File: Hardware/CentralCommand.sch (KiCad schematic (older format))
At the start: 15 parts, among them IC101 STM32F030C8, P101 SERIAL, P102 I2C, P103 SPI, P104 ADC, Y101 Crystal_Small

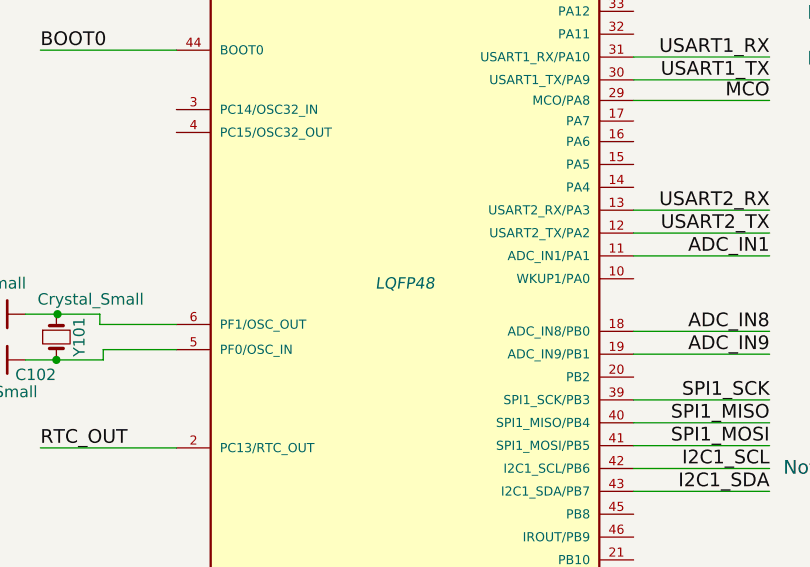
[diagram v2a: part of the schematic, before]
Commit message: initial footprint assignments
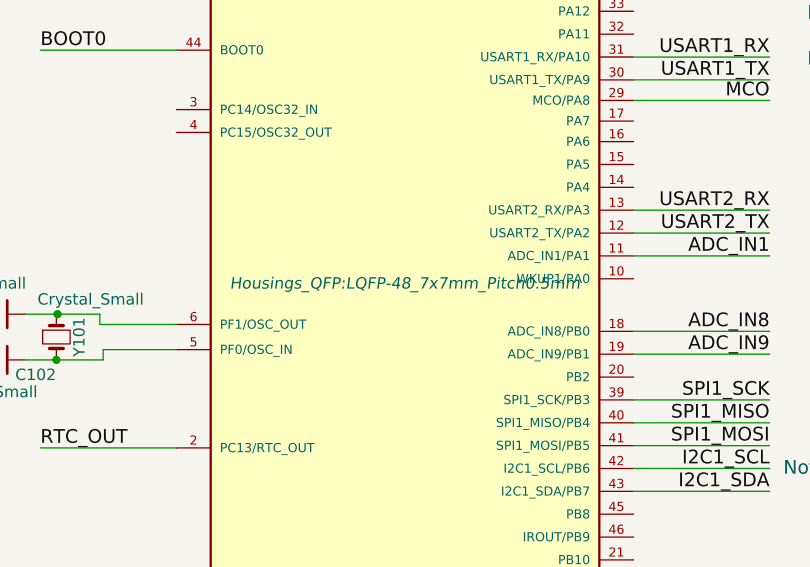
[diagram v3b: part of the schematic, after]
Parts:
- C101, C102, C104, C105, C106, C108: footprint (none) -> Capacitors_SMD:C_0805
- C103, C107: footprint (none) -> Capacitors_SMD:C_1206
- IC101: footprint LQFP48 -> Housings_QFP:LQFP-48_7x7mm_Pitch0.5mm
- P101, P102: footprint (none) -> Pin_Headers:Pin_Header_Straight_1x02
- P103, P104: footprint (none) -> Pin_Headers:Pin_Header_Straight_1x04
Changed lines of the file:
@@
 F 0 "C107" H 3580 1970 50  0000 L CNN
 F 1 "10nF" H 3580 1820 50  0000 L CNN
-F 2 "" H 3570 1900 50  0000 C CNN
+F 2 "Capacitors_SMD:C_1206" H 3570 1900 50  0001 C CNN
 F 3 "" H 3570 1900 50  0000 C CNN
 F 4 "Value" H 3570 1900 60  0001 C CNN "Fieldname"
@@
 $EndComp
 $Comp
-L GND #PWR107
+L GND #PWR01
 U 1 1 58D7B611
 P 3570 2070
-F 0 "#PWR107" H 3570 1820 50  0001 C CNN
+F 0 "#PWR01" H 3570 1820 50  0001 C CNN
 F 1 "GND" H 3570 1920 50  0000 C CNN
 F 2 "" H 3570 2070 50  0000 C CNN
@@
 F 0 "Y101" H 1445 4605 50  0000 C CNN
 F 1 "Crystal_Small" V 1280 4655 50  0000 C CNN
-F 2 "" H 1445 4505 50  0000 C CNN
+F 2 "" H 1445 4505 50  0001 C CNN
 F 3 "" H 1445 4505 50  0000 C CNN
 	1    1445 4505
@@
 F 0 "C101" V 1190 4195 50  0000 L CNN
 F 1 "C_Small" V 1075 4235 50  0000 L CNN
-F 2 "" H 1210 4405 50  0000 C CNN
+F 2 "Capacitors_SMD:C_0805" H 1210 4405 50  0001 C CNN
 F 3 "" H 1210 4405 50  0000 C CNN
 	1    1210 4405
@@
 F 0 "C102" V 1275 4660 50  0000 L CNN
 F 1 "C_Small" V 1350 4485 50  0000 L CNN
-F 2 "" H 1210 4605 50  0000 C CNN
+F 2 "Capacitors_SMD:C_0805" H 1210 4605 50  0001 C CNN
 F 3 "" H 1210 4605 50  0000 C CNN
 	1    1210 4605
@@
 Connection ~ 1450 4405
 $Comp
-L GND #PWR101
+L GND #PWR02
 U 1 1 58D7BBA2
 P 905 4550
-F 0 "#PWR101" H 905 4300 50  0001 C CNN
+F 0 "#PWR02" H 905 4300 50  0001 C CNN
 F 1 "GND" H 905 4400 50  0000 C CNN
 F 2 "" H 905 4550 50  0000 C CNN
@@
 $EndComp
 $Comp
-L GND #PWR106
+L GND #PWR03
 U 1 1 58D7BD5D
 P 2890 6605
-F 0 "#PWR106" H 2890 6355 50  0001 C CNN
+F 0 "#PWR03" H 2890 6355 50  0001 C CNN
 F 1 "GND" H 2890 6455 50  0000 C CNN
 F 2 "" H 2890 6605 50  0000 C CNN
@@
 F 0 "C108" H 3920 1970 50  0000 L CNN
 F 1 "1uF" H 3920 1820 50  0000 L CNN
-F 2 "" H 3910 1900 50  0000 C CNN
+F 2 "Capacitors_SMD:C_0805" H 3910 1900 50  0001 C CNN
 F 3 "" H 3910 1900 50  0000 C CNN
 F 4 "Value" H 3910 1900 60  0001 C CNN "Fieldname"
@@
 $EndComp
 $Comp
-L GND #PWR108
+L GND #PWR04
 U 1 1 58D8537A
 P 3910 2080
-F 0 "#PWR108" H 3910 1830 50  0001 C CNN
+F 0 "#PWR04" H 3910 1830 50  0001 C CNN
 F 1 "GND" H 3910 1930 50  0000 C CNN
 F 2 "" H 3910 2080 50  0000 C CNN
@@
 F 0 "L101" V 2825 1750 50  0000 L CNN
 F 1 "40nH" V 3070 1720 50  0000 L CNN
-F 2 "" V 2870 1800 50  0000 C CNN
+F 2 "" V 2870 1800 50  0001 C CNN
 F 3 "" H 2940 1800 50  0000 C CNN
 F 4 "Value" H 2940 1800 60  0001 C CNN "Fieldname"
@@
 F 0 "C105" H 1985 1970 50  0000 L CNN
 F 1 "0.1uF" H 1985 1820 50  0000 L CNN
-F 2 "" H 1975 1900 50  0000 C CNN
+F 2 "Capacitors_SMD:C_0805" H 1975 1900 50  0001 C CNN
 F 3 "" H 1975 1900 50  0000 C CNN
 F 4 "Value" H 1975 1900 60  0001 C CNN "Fieldname"
@@
 $EndComp
 $Comp
-L GND #PWR104
+L GND #PWR05
 U 1 1 58D85B9E
 P 1975 2070
-F 0 "#PWR104" H 1975 1820 50  0001 C CNN
+F 0 "#PWR05" H 1975 1820 50  0001 C CNN
 F 1 "GND" H 1975 1920 50  0000 C CNN
 F 2 "" H 1975 2070 50  0000 C CNN
@@
 F 0 "C106" H 2260 1970 50  0000 L CNN
 F 1 "0.1uF" H 2260 1820 50  0000 L CNN
-F 2 "" H 2250 1900 50  0000 C CNN
+F 2 "Capacitors_SMD:C_0805" H 2250 1900 50  0001 C CNN
 F 3 "" H 2250 1900 50  0000 C CNN
 F 4 "Value" H 2250 1900 60  0001 C CNN "Fieldname"
@@
 $EndComp
 $Comp
-L GND #PWR105
+L GND #PWR06
 U 1 1 58D85BAC
 P 2250 2080
-F 0 "#PWR105" H 2250 1830 50  0001 C CNN
+F 0 "#PWR06" H 2250 1830 50  0001 C CNN
 F 1 "GND" H 2250 1930 50  0000 C CNN
 F 2 "" H 2250 2080 50  0000 C CNN
@@
 F 0 "C104" H 1710 1970 50  0000 L CNN
 F 1 "0.1uF" H 1710 1820 50  0000 L CNN
-F 2 "" H 1700 1900 50  0000 C CNN
+F 2 "Capacitors_SMD:C_0805" H 1700 1900 50  0001 C CNN
 F 3 "" H 1700 1900 50  0000 C CNN
 F 4 "Value" H 1700 1900 60  0001 C CNN "Fieldname"
@@
 $EndComp
 $Comp
-L GND #PWR103
+L GND #PWR07
 U 1 1 58D85FE3
 P 1700 2070
-F 0 "#PWR103" H 1700 1820 50  0001 C CNN
+F 0 "#PWR07" H 1700 1820 50  0001 C CNN
 F 1 "GND" H 1700 1920 50  0000 C CNN
 F 2 "" H 1700 2070 50  0000 C CNN
@@
 F 0 "C103" H 1455 1970 50  0000 L CNN
 F 1 "4.7uF" H 1455 1820 50  0000 L CNN
-F 2 "" H 1445 1900 50  0000 C CNN
+F 2 "Capacitors_SMD:C_1206" H 1445 1900 50  0001 C CNN
 F 3 "" H 1445 1900 50  0000 C CNN
 F 4 "Value" H 1445 1900 60  0001 C CNN "Fieldname"
@@
 $EndComp
 $Comp
-L GND #PWR102
+L GND #PWR08
 U 1 1 58D86305
 P 1445 2070
-F 0 "#PWR102" H 1445 1820 50  0001 C CNN
+F 0 "#PWR08" H 1445 1820 50  0001 C CNN
 F 1 "GND" H 1445 1920 50  0000 C CNN
 F 2 "" H 1445 2070 50  0000 C CNN
@@
 F 0 "P101" H 10685 1170 50  0000 C CNN
 F 1 "SERIAL" V 10785 1020 50  0000 C CNN
-F 2 "" H 10685 1020 50  0000 C CNN
+F 2 "Pin_Headers:Pin_Header_Straight_1x02" H 10685 1020 50  0001 C CNN
 F 3 "" H 10685 1020 50  0000 C CNN
 F 4 "Value" H 10685 1020 60  0001 C CNN "Fieldname"
@@
 F 0 "P103" H 10695 1925 50  0000 C CNN
 F 1 "SPI" V 10795 1675 50  0000 C CNN
-F 2 "" H 10695 1675 50  0000 C CNN
+F 2 "Pin_Headers:Pin_Header_Straight_1x04" H 10695 1675 50  0001 C CNN
 F 3 "" H 10695 1675 50  0000 C CNN
 F 4 "Value" H 10695 1675 60  0001 C CNN "Fieldname"
@@
 F 0 "P104" H 10700 2735 50  0000 C CNN
 F 1 "ADC" V 10800 2485 50  0000 C CNN
-F 2 "" H 10700 2485 50  0000 C CNN
+F 2 "Pin_Headers:Pin_Header_Straight_1x04" H 10700 2485 50  0001 C CNN
 F 3 "" H 10700 2485 50  0000 C CNN
 F 4 "Value" H 10700 2485 60  0001 C CNN "Fieldname"
@@
 ADC HEADER
 $Comp
-L GND #PWR109
+L GND #PWR09
 U 1 1 58DE92ED
 P 10355 2635
-F 0 "#PWR109" H 10355 2385 50  0001 C CNN
+F 0 "#PWR09" H 10355 2385 50  0001 C CNN
 F 1 "GND" H 10355 2485 50  0000 C CNN
 F 2 "" H 10355 2635 50  0000 C CNN
@@
 F 0 "P102" H 10690 3565 50  0000 C CNN
 F 1 "I2C" V 10790 3415 50  0000 C CNN
-F 2 "" H 10690 3415 50  0000 C CNN
+F 2 "Pin_Headers:Pin_Header_Straight_1x02" H 10690 3415 50  0001 C CNN
 F 3 "" H 10690 3415 50  0000 C CNN
 F 4 "Value" H 10690 3415 60  0001 C CNN "Fieldname"
@@
 F 0 "IC101" H 2120 6150 50  0000 L BNN
 F 1 "STM32F030C8" H 3370 2320 50  0000 L BNN
-F 2 "LQFP48" H 2970 4270 50  0000 C CIN
+F 2 "Housings_QFP:LQFP-48_7x7mm_Pitch0.5mm" H 2970 4270 50  0000 C CIN
 F 3 "http://www.st.com/content/ccc/resource/technical/document/datasheet/a4/5d/0b/0e/87/c4/4d/71/DM00088500.pdf/files/DM00088500.pdf/jcr:content/translations/en.DM00088500.pdf" H 2970 4270 50  0001 C CNN
 F 4 "Value" H 2970 4270 60  0001 C CNN "Fieldname"

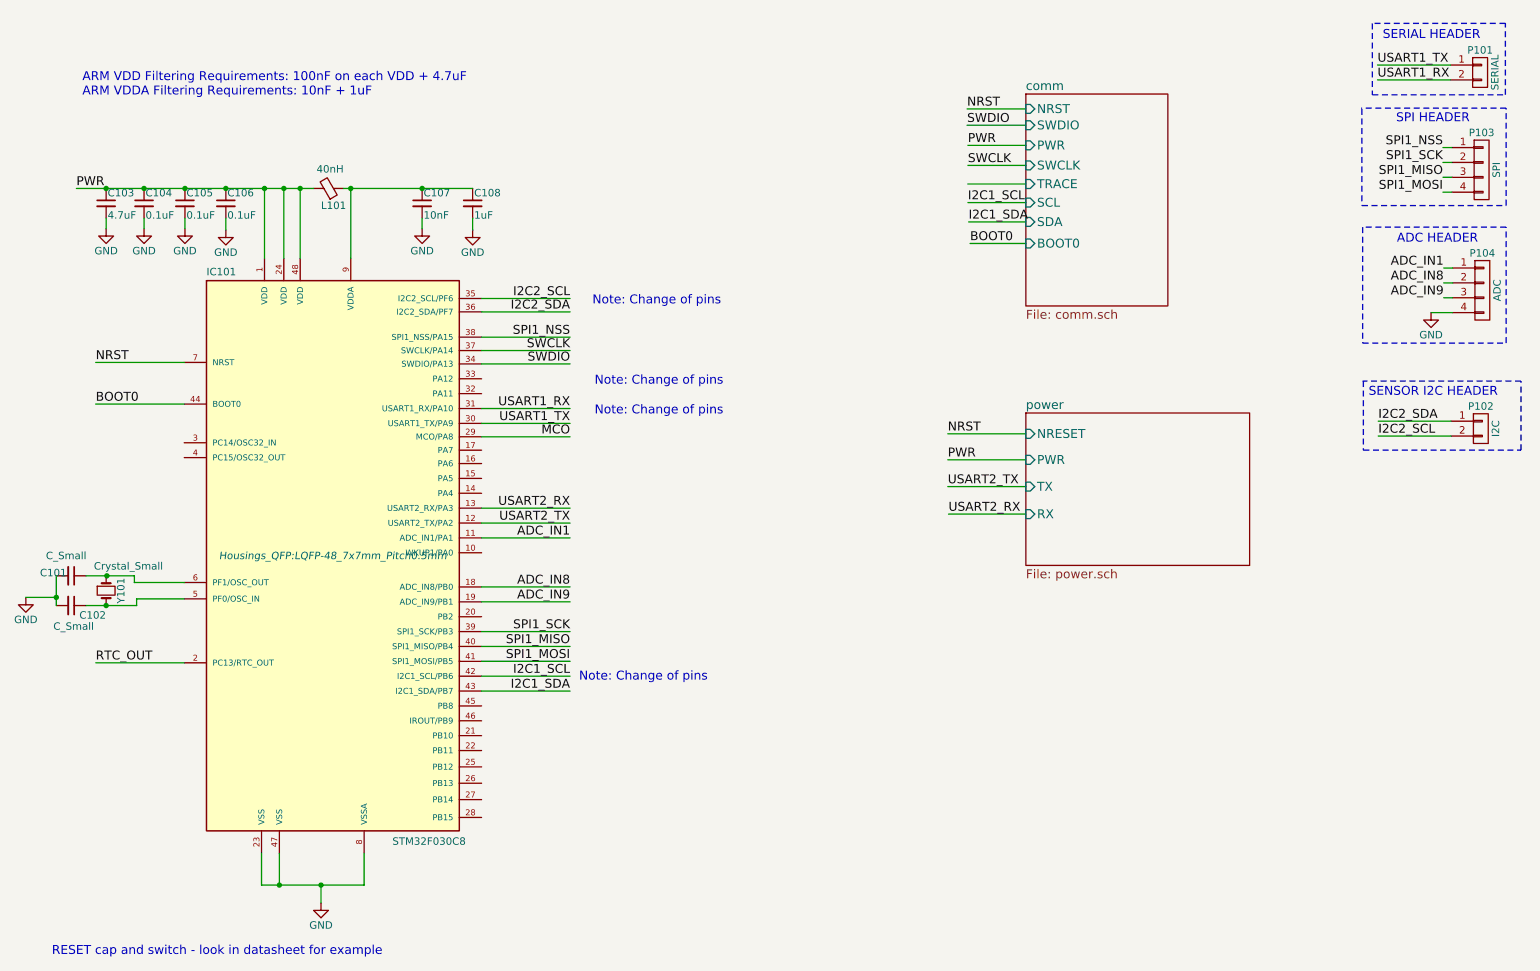
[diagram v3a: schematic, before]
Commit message: added crystal details and usb footprint
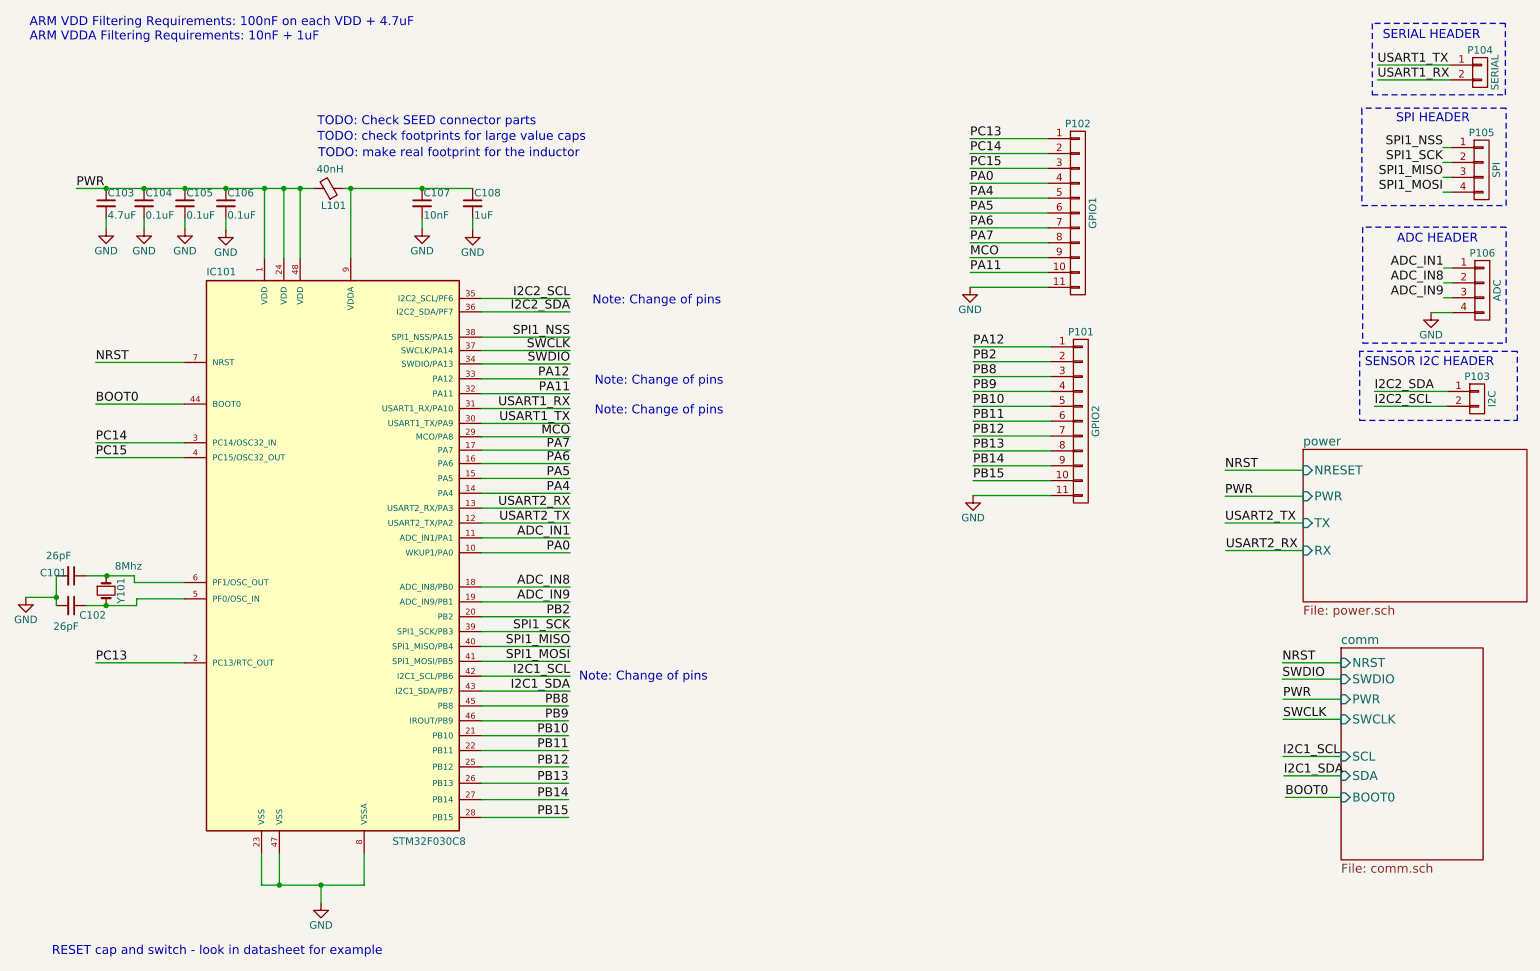
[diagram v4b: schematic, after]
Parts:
- added P101: GPIO2, Pin_Headers:Pin_Header_Straight_1x11, symbol CONN_01X11
- added P102: GPIO1, Pin_Headers:Pin_Header_Straight_1x11, symbol CONN_01X11
- C101, C102: value C_Small -> 26pF; Fieldname (none) -> Value
- IC101: MPN (none) -> STM32F030C8T6
- L101: footprint (none) -> Capacitors_SMD:C_0805; MPN (none) -> MI0805K400R-10
- Y101: value Crystal_Small -> 8Mhz; Fieldname (none) -> Value; MPN (none) -> 9C-8.000MEEJ-T; Note (none) -> 18pF load capacitance
- renumbered P102 to P103, P101 to P104, P103 to P105, P104 to P106
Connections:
- net GND: now also P101.11 (P11), P102.11 (P11)
- net MCO: now also P102.9 (P9)
- net PA0: now reaches IC101.10 (WKUP1/PA0)
- net PA0: now also P102.4 (P4)
- net PA4: now reaches IC101.14 (PA4)
- net PA4: now also P102.5 (P5)
- net PA5: now reaches IC101.15 (PA5)
- net PA5: now also P102.6 (P6)
- net PA6: now reaches IC101.16 (PA6)
- net PA6: now also P102.7 (P7)
- net PA7: now reaches IC101.17 (PA7)
- net PA7: now also P102.8 (P8)
- net PB2: now reaches IC101.20 (PB2)
- net PB2: now also P101.2 (P2)
- net PB10: now reaches IC101.21 (PB10)
- net PB10: now also P101.5 (P5)
- net PB11: now reaches IC101.22 (PB11)
- net PB11: now also P101.6 (P6)
- net PB12: now reaches IC101.25 (PB12)
- net PB12: now also P101.7 (P7)
- net PB13: now reaches IC101.26 (PB13)
- net PB13: now also P101.8 (P8)
- net PB14: now reaches IC101.27 (PB14)
- net PB14: now also P101.9 (P9)
- net PB15: now reaches IC101.28 (PB15)
- net PB15: now also P101.10 (P10)
- net PC14: now reaches IC101.3 (PC14/OSC32_IN)
- net PC14: now also P102.2 (P2)
- net PA11: now reaches IC101.32 (PA11)
- net PA11: now also P102.10 (P10)
- net PA12: now reaches IC101.33 (PA12)
- net PA12: now also P101.1 (P1)
- net PC15: now reaches IC101.4 (PC15/OSC32_OUT)
- net PC15: now also P102.3 (P3)
- net PB8: now reaches IC101.45 (PB8)
- net PB8: now also P101.3 (P3)
- net PB9: now reaches IC101.46 (IROUT/PB9)
- net PB9: now also P101.4 (P4)
- net RTC_OUT renamed PC13
- net PC13: now also P102.1 (P1)
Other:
- note added: "TODO: Check SEED connector parts"
- note added: "TODO: check footprints for large value caps"
- note added: "TODO: make real footprint for the inductor"
- moved on the sheet: P103

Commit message: changed grove connectors to jst sh and added VCC and GND to other headers
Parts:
- removed P101: GPIO2, Pin_Headers:Pin_Header_Straight_1x11, symbol CONN_01X11
- removed P102: GPIO1, Pin_Headers:Pin_Header_Straight_1x11, symbol CONN_01X11
- removed P103: I2C, Pin_Headers:Pin_Header_Straight_1x02, symbol CONN_01X02
- removed P104: SERIAL, Pin_Headers:Pin_Header_Straight_1x02, symbol CONN_01X02
- removed P105: SPI, Pin_Headers:Pin_Header_Straight_1x04, symbol CONN_01X04
- added P101: I2C, Pin_Headers:Pin_Header_Straight_1x04, symbol CONN_01X04
- added P102, P103: GPIO1, Pin_Headers:Pin_Header_Straight_1x12, symbol CONN_01X12
- added P104: USART, Pin_Headers:Pin_Header_Straight_1x04, symbol CONN_01X04
- added P105: SPI, Pin_Headers:Pin_Header_Straight_1x06, symbol CONN_01X06
- Y101: footprint (none) -> Crystals:Crystal_HC49-SD_SMD
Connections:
- net GND: now also P101.1 (P1), P102.1 (P1), P103.1 (P1), P104.1 (P1), P105.1 (P1)
- net I2C2_SCL: now also P101.3 (P3)
- net I2C2_SDA: now also P101.4 (P4)
- net MCO: now also P102.11 (P11)
- net PA0: now also P102.6 (P6)
- net PA11: now also P102.12 (P12)
- net PA12: now also P103.3 (P3)
- net PA4: now also P102.7 (P7)
- net PA5: now also P102.8 (P8)
- net PA6: now also P102.9 (P9)
- net PA7: now also P102.10 (P10)
- net PB10: now also P103.7 (P7)
- net PB11: now also P103.8 (P8)
- net PB12: now also P103.9 (P9)
- net PB13: now also P103.10 (P10)
- net PB14: now also P103.11 (P11)
- net PB15: now also P103.12 (P12)
- net PB2: now also P103.4 (P4)
- net PB8: now also P103.5 (P5)
- net PB9: now also P103.6 (P6)
- net PC13: now also P102.3 (P3)
- net PC14: now also P102.4 (P4)
- net PC15: now also P102.5 (P5)
- net PWR: now also P101.2 (P2), P102.2 (P2), P103.2 (P2), P104.2 (P2), P105.2 (P2)
- net SPI1_MISO: now also P105.4 (P4)
- net SPI1_MOSI: now also P105.3 (P3)
- net SPI1_NSS: now also P105.6 (P6)
- net SPI1_SCK: now also P105.5 (P5)
- net USART1_RX: now also P104.3 (P3)
- net USART1_TX: now also P104.4 (P4)
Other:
- moved on the sheet: P106

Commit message: fixed jst sh headers and added button footprint
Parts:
- C103: footprint Capacitors_SMD:C_1206 -> Capacitors_SMD:C_0805
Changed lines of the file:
@@
 F 0 "C103" H 1455 1970 50  0000 L CNN
 F 1 "4.7uF" H 1455 1820 50  0000 L CNN
-F 2 "Capacitors_SMD:C_1206" H 1445 1900 50  0001 C CNN
+F 2 "Capacitors_SMD:C_0805" H 1445 1900 50  0001 C CNN
 F 3 "" H 1445 1900 50  0000 C CNN
 F 4 "Value" H 1445 1900 60  0001 C CNN "Fieldname"

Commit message: started board layout
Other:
- note removed: "TODO: Check SEED connector parts"
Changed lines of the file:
@@
 Wire Wire Line
 	9495 4235 8975 4235
+Text Label 8975 4235 0    60   ~ 0
+USART2_TX
 Text Label 8970 4050 0    60   ~ 0
-USART2_TX
-Text Label 8975 4235 0    60   ~ 0
 USART2_RX
 Text Label 8970 3695 0    60   ~ 0
@@
 Text Notes 2865 1490 0    60   ~ 0
 TODO: check footprints for large value caps
-Text Notes 2865 1385 0    60   ~ 0
-TODO: Check SEED connector parts
 $Comp
 L CONN_01X04 P101

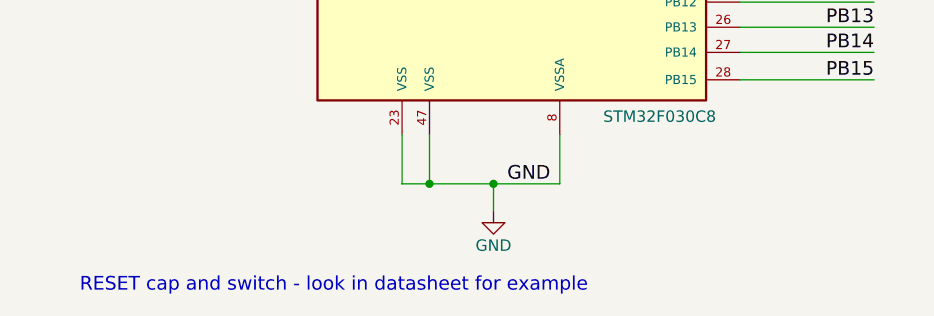
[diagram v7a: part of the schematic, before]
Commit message: converted VCCIO to 3V3 and added 1x2 power and gnd
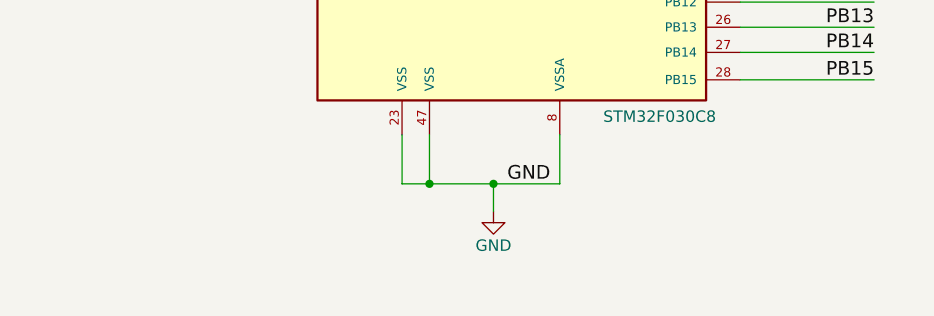
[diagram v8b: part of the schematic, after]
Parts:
- C107: footprint Capacitors_SMD:C_1206 -> Capacitors_SMD:C_0805
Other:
- note removed: "RESET cap and switch - look in datasheet for example"
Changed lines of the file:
@@
 F 0 "C107" H 3580 1970 50  0000 L CNN
 F 1 "10nF" H 3580 1820 50  0000 L CNN
-F 2 "Capacitors_SMD:C_1206" H 3570 1900 50  0001 C CNN
+F 2 "Capacitors_SMD:C_0805" H 3570 1900 50  0001 C CNN
 F 3 "" H 3570 1900 50  0000 C CNN
 F 4 "Value" H 3570 1900 60  0001 C CNN "Fieldname"
@@
 	905  4550 1110 4550
 Connection ~ 1110 4550
-Text Notes 1080 6965 0    60   ~ 0
-RESET cap and switch - look in datasheet for example
 $Comp
 L C_Small C108
